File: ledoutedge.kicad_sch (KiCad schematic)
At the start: 9 parts, among them J801 Conn_02x06_Odd_Even

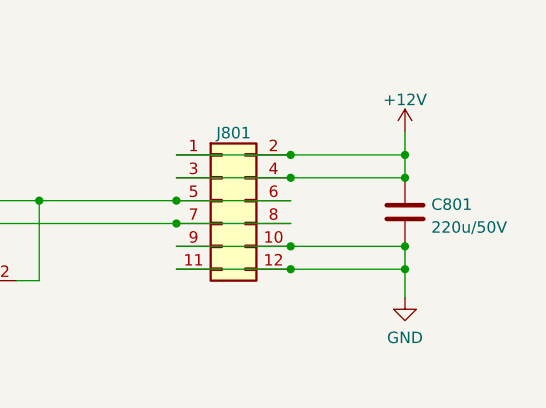
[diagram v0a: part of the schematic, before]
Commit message: Fix DRCs and BOM errors
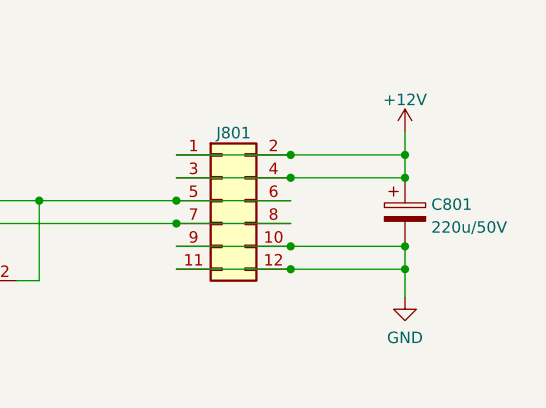
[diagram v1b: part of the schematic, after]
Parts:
- C801: symbol Device:C -> Device:C_Polarized
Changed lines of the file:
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@@
     (pin "2")
   )
-  (symbol (lib_id "Device:C") (at 182.88 87.63 0) (unit 1)
+  (symbol (lib_id "Device:C_Polarized") (at 182.88 87.63 0) (unit 1)
     (in_bom yes) (on_board yes) (fields_autoplaced)
     (property "Reference" "C801" (id 0) (at 185.801 86.7953 0)
